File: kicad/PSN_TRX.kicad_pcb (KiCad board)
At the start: 4 copper layers, 220 x 150 mm, 161 parts, among them IC1 LP2950L-5.0V, IC2 NJM2904, J1 PWR_IN, K1 G5V-2, Q1 3SK59, Q10 2SK439, Q11 2SC1815, Q12 2SC1815, Q13 2SC1815, Q14 2SK439, Q15 2SC1815, Q17 2SC1815, Q2 2SC1923, Q3 2SC1815, Q4 2SC1815, Q5 2SC2120, Q6 2SA950, Q7 2SC1923, Q8 2SC1923, Q9 2SK439, SW1 SW, T1 ST-71, X1 50.5MHz/3

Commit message: KiCad: シンボル統合・パネル部品除外・PCBクリーンアップ
- 外部シンボルファイル4本をPSN_TRX.kicad_symに統合
  (Arduino_Nano_R4_Socket, Si5351_DIP8, Si5351A, AE-LCNV4-MOSFET)
  → sym-lib-tableはPSN_TRXライブラリのみに統一
- SW1, SW2, R13, LED1をon_board=noに変更（パネル取付部品）
- PCBからSW1, R13, LED1フットプリントを削除（SW2は元から未配置）
- .gitignoreに_restore_backup_*/を追加

Co-Authored-By: Claude Sonnet 4.6 <noreply@anthropic.com>
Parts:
- removed LED1: LED, PinHeader_1x02_P2.54mm_Vertical
- removed R13: 1k, R_Axial_DIN0207_L6.3mm_D2.5mm_P2.54mm_Vertical
- removed SW1: SW, SW_DIP_SPSTx01_Slide_6.7x4.1mm_W7.62mm_P2.54mm_LowProfile

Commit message: KiCad: VR1・VR2をパネル取付に変更（on_board=no、PCBから削除）
Co-Authored-By: Claude Sonnet 4.6 <noreply@anthropic.com>
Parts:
- removed VR1: 5k, PinHeader_1x03_P2.54mm_Vertical
- removed VR2: 10k, PinHeader_1x03_P2.54mm_Vertical

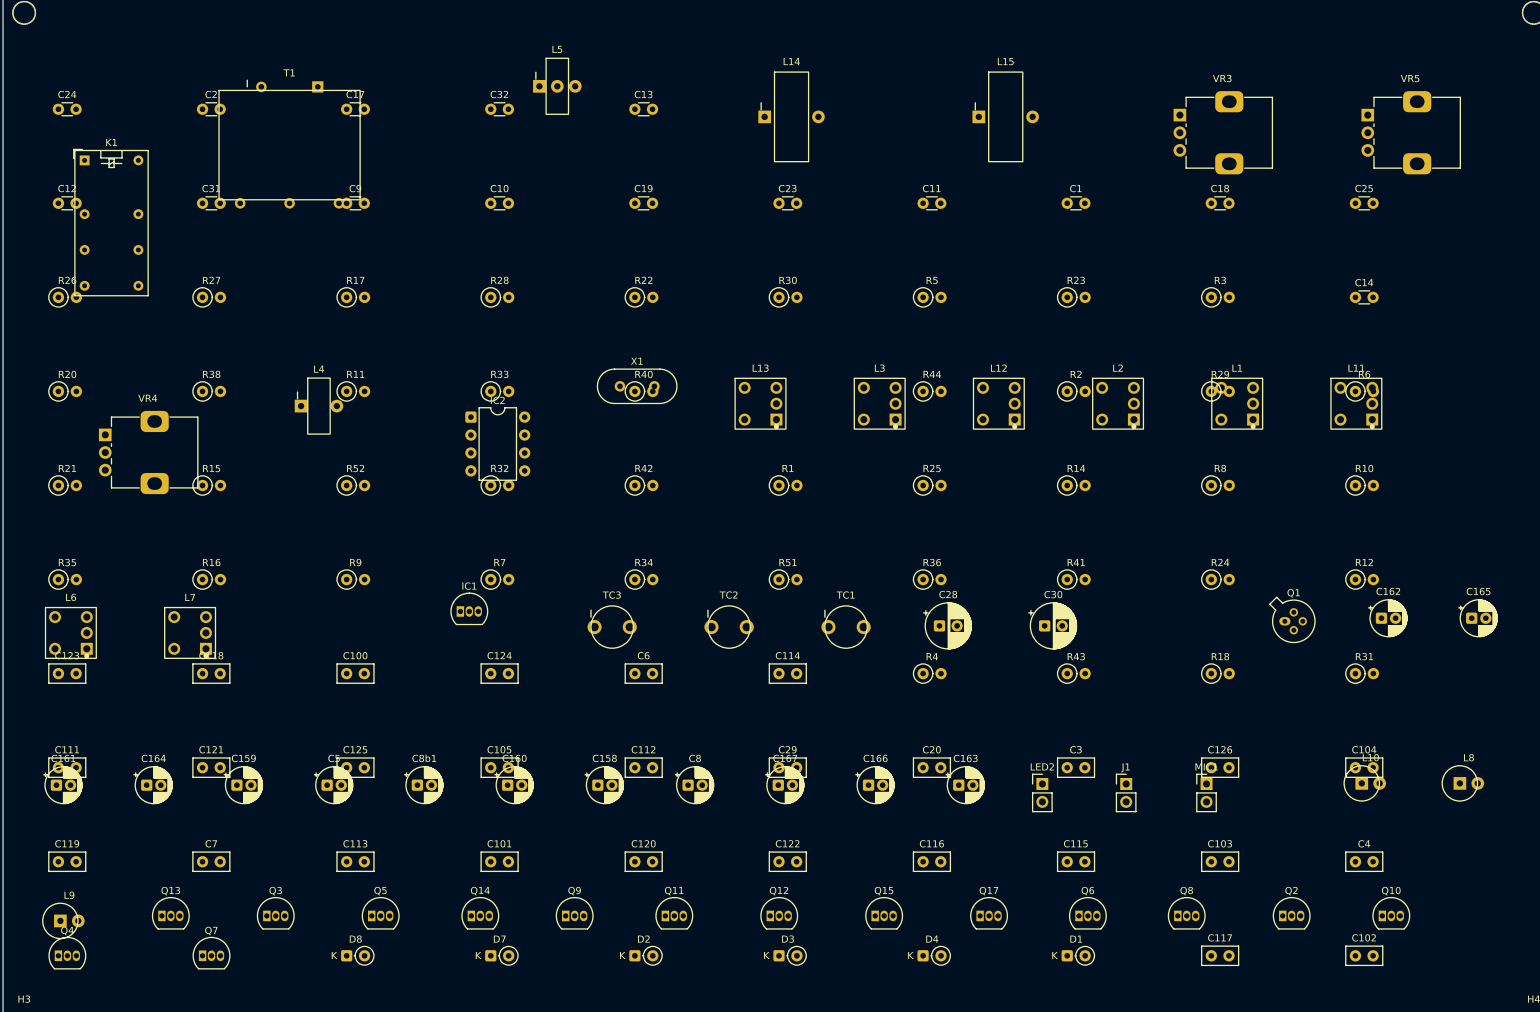
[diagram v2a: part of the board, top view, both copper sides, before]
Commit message: feat: GF063Pポテンショメータのカスタムシンボル追加・フットプリント修正、VR3-7をPSN_TRXライブラリに移行
- PSN_TRX:Potentiometer_GF063P シンボルをシンボルライブラリに追加（VRプレフィックス、フットプリント紐付け済み）
- Potentiometer_TOCOS_GF063P_Vertical フットプリントのピン配置をデータシートに基づき修正
  - 旧: ピン1・2・3が一直線（誤り）
  - 新: 三角配置（ピン2ワイパーを2.5mm上方にオフセット）
- VR3〜VR7のシンボル参照を Device:R_Potentiometer → PSN_TRX:Potentiometer_GF063P に変更

Co-Authored-By: Claude Sonnet 4.6 <noreply@anthropic.com>
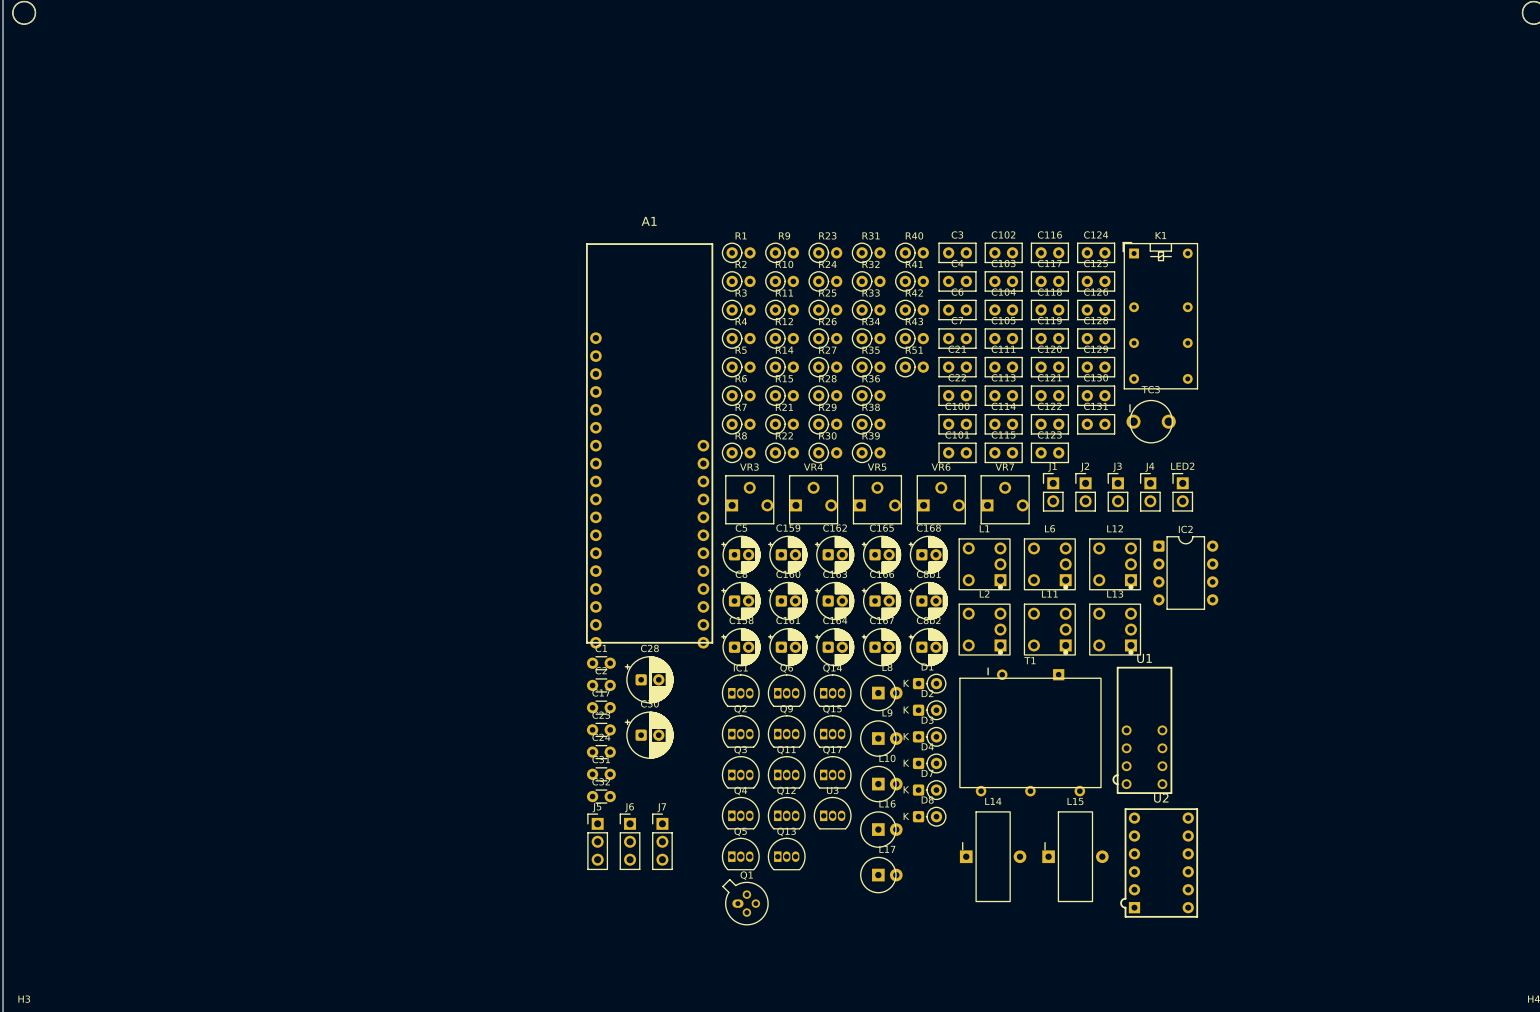
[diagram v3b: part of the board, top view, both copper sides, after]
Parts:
- removed C10, C9: 100p, C_Disc_D3.0mm_W1.6mm_P2.50mm
- removed C11, C12, C14: 47p, C_Disc_D3.0mm_W1.6mm_P2.50mm
- removed C112: 0.01u, C_Disc_D5.0mm_W2.5mm_P2.50mm
- removed C13: 5p, C_Disc_D3.0mm_W1.6mm_P2.50mm
- removed C18: 15p, C_Disc_D3.0mm_W1.6mm_P2.50mm
- removed C19, C25: 33p, C_Disc_D3.0mm_W1.6mm_P2.50mm
- removed C20, C29: 0.001u, C_Disc_D5.0mm_W2.5mm_P2.50mm
- removed L3, L7: 7T50, L_FCZ07S_CT
- removed L4: T-30-10 6T/0.4mm, L_T30_2pin_Vertical
- removed L5: T-30-10 6T+1T/0.4mm, L_T30_3pin_Vertical
- removed MIC1: MIC, PinHeader_1x02_P2.54mm_Vertical
- removed Q10: 2SK439, TO-92_Inline
- removed Q7, Q8: 2SC1923, TO-92_Inline
- removed R16: 10k, R_Axial_DIN0207_L6.3mm_D2.5mm_P2.54mm_Vertical
- removed R17, R20: 100k, R_Axial_DIN0207_L6.3mm_D2.5mm_P2.54mm_Vertical
- removed R18: 1k, R_Axial_DIN0207_L6.3mm_D2.5mm_P2.54mm_Vertical
- removed R44: 100, R_Axial_DIN0207_L6.3mm_D2.5mm_P2.54mm_Vertical
- removed R52: 51, R_Axial_DIN0207_L6.3mm_D2.5mm_P2.54mm_Vertical
- removed TC1, TC2: 40p, C_Trimmer_TMCV01
- removed X1: 50.5MHz/3, Crystal_HC49-4H_Vertical
- added A1: Arduino_Nano_R4_Socket, PSN_TRX:Arduino_Nano_R4_Socket, F.Cu at (96.7, 69.4)
- added C128: 47PF, Capacitor_THT:C_Disc_D5.0mm_W2.5mm_P2.50mm, F.Cu at (158.7, 54.2)
- added C129: 47PF, Capacitor_THT:C_Disc_D5.0mm_W2.5mm_P2.50mm, F.Cu at (158.7, 58.2)
- added C130: 47PF, Capacitor_THT:C_Disc_D5.0mm_W2.5mm_P2.50mm, F.Cu at (158.7, 62.3)
- added C131: 47PF, Capacitor_THT:C_Disc_D5.0mm_W2.5mm_P2.50mm, F.Cu at (158.7, 66.3)
- added C168: 1u, Capacitor_THT:CP_Radial_D5.0mm_P2.00mm, F.Cu at (135.3, 84.8)
- added C21: 0.001u, Capacitor_THT:C_Disc_D5.0mm_W2.5mm_P2.50mm, F.Cu at (139.1, 58.2)
- added C22: 0.001u, Capacitor_THT:C_Disc_D5.0mm_W2.5mm_P2.50mm, F.Cu at (139.1, 62.3)
- added C8b2: 10u, Capacitor_THT:CP_Radial_D5.0mm_P2.00mm, F.Cu at (135.3, 97.9)
- added J2: SP-OUT, Connector_PinHeader_2.54mm:PinHeader_1x02_P2.54mm_Vertical, F.Cu at (158.5, 74.7)
- added J3: RF-IN, Connector_PinHeader_2.54mm:PinHeader_1x02_P2.54mm_Vertical, F.Cu at (163.1, 74.7)
- added J4: MIC-IN, Connector_PinHeader_2.54mm:PinHeader_1x02_P2.54mm_Vertical, F.Cu at (167.6, 74.7)
- added J5: I2C_OUT, Connector_PinHeader_2.54mm:PinHeader_1x03_P2.54mm_Vertical, F.Cu at (89.3, 123.0)
- added J6: Volume, Connector_PinHeader_2.54mm:PinHeader_1x03_P2.54mm_Vertical, F.Cu at (93.9, 123.0)
- added J7: Volume, Connector_PinHeader_2.54mm:PinHeader_1x03_P2.54mm_Vertical, F.Cu at (98.5, 123.0)
- added L16: 100nH, PSN_TRX:L_AL0510-153K_Vertical, F.Cu at (129.1, 123.8)
- added L17: 100nH, PSN_TRX:L_AL0510-153K_Vertical, F.Cu at (129.1, 130.2)
- added R39: 51, Resistor_THT:R_Axial_DIN0207_L6.3mm_D2.5mm_P2.54mm_Vertical, F.Cu at (126.8, 70.4)
- added U1: Si5351_DIP8, PSN_TRX:DIP-8_W7.62mm, F.Cu at (166.8, 109.7)
- added U2: AE-LCNV4-MOSFET, PSN_TRX:DIP-12_W7.62mm, F.Cu at (169.2, 122.1)
- added U3: LP2950-3.3_TO92, Package_TO_SOT_THT:TO-92_Inline, F.Cu at (121.3, 121.8)
- added VR6: 500, PSN_TRX:Potentiometer_TOCOS_GF063P_Vertical, F.Cu at (135.5, 77.8)
- added VR7: 500, PSN_TRX:Potentiometer_TOCOS_GF063P_Vertical, F.Cu at (144.6, 77.8)
- C1, C17, C2, C23, C24, C31, C32: footprint C_Disc_D3.0mm_W1.6mm_P2.50mm -> Capacitor_THT:C_Disc_D3.0mm_W1.6mm_P2.50mm
- C100, C101, C103, C111, C113, C114, C115, C116, C117, C118, C119, C120, C121, C124, C125, C126, C3, C4, C6, C7: footprint C_Disc_D5.0mm_W2.5mm_P2.50mm -> Capacitor_THT:C_Disc_D5.0mm_W2.5mm_P2.50mm
- C102, C104, C105, C122, C123: value 0.01u -> 1u; footprint C_Disc_D5.0mm_W2.5mm_P2.50mm -> Capacitor_THT:C_Disc_D5.0mm_W2.5mm_P2.50mm
- C158, C159, C160, C161, C162, C163, C164, C165, C166, C167, C5, C8, C8b1: footprint CP_Radial_D5.0mm_P2.00mm -> Capacitor_THT:CP_Radial_D5.0mm_P2.00mm
- C28, C30: footprint CP_Radial_D6.3mm_P2.50mm -> Capacitor_THT:CP_Radial_D6.3mm_P2.50mm
- D1, D2, D3, D4, D7, D8: footprint D_DO-35_SOD27_P2.54mm_Vertical_CathodeUp -> Diode_THT:D_DO-35_SOD27_P2.54mm_Vertical_CathodeUp
- IC1, Q11, Q12, Q13, Q14, Q15, Q17, Q2, Q3, Q4, Q5, Q6, Q9: footprint TO-92_Inline -> Package_TO_SOT_THT:TO-92_Inline
- IC2: footprint DIP-8_W7.62mm -> Package_DIP:DIP-8_W7.62mm
- J1, LED2: footprint PinHeader_1x02_P2.54mm_Vertical -> Connector_PinHeader_2.54mm:PinHeader_1x02_P2.54mm_Vertical
- K1: footprint Relay_DPDT_Omron_G5V-2 -> Relay_THT:Relay_DPDT_Omron_G5V-2
- L1, L11, L12, L13, L2, L6: footprint L_FCZ07S_CT -> PSN_TRX:L_FCZ07S_CT
- L10, L8, L9: footprint L_AL0510-153K_Vertical -> PSN_TRX:L_AL0510-153K_Vertical
- L14, L15: footprint L_T50_2pin_Vertical -> PSN_TRX:L_T50_2pin_Vertical
- Q1: footprint TO-72-4 -> Package_TO_SOT_THT:TO-72-4
- R1, R10, R11, R12, R14, R15, R2, R22, R23, R24, R25, R26, R27, R3, R33, R35, R36, R38, R4, R40, R41, R42, R43, R5, R51, R6, R7, R8, R9: footprint R_Axial_DIN0207_L6.3mm_D2.5mm_P2.54mm_Vertical -> Resistor_THT:R_Axial_DIN0207_L6.3mm_D2.5mm_P2.54mm_Vertical
- R21: value 220k -> 47; footprint R_Axial_DIN0207_L6.3mm_D2.5mm_P2.54mm_Vertical -> Resistor_THT:R_Axial_DIN0207_L6.3mm_D2.5mm_P2.54mm_Vertical
- R28, R31: value 100k -> 1M; footprint R_Axial_DIN0207_L6.3mm_D2.5mm_P2.54mm_Vertical -> Resistor_THT:R_Axial_DIN0207_L6.3mm_D2.5mm_P2.54mm_Vertical
- R29: value 330 -> 4.7k; footprint R_Axial_DIN0207_L6.3mm_D2.5mm_P2.54mm_Vertical -> Resistor_THT:R_Axial_DIN0207_L6.3mm_D2.5mm_P2.54mm_Vertical
- R30: value 1k -> 330; footprint R_Axial_DIN0207_L6.3mm_D2.5mm_P2.54mm_Vertical -> Resistor_THT:R_Axial_DIN0207_L6.3mm_D2.5mm_P2.54mm_Vertical
- R32: value 1k -> 4.7k; footprint R_Axial_DIN0207_L6.3mm_D2.5mm_P2.54mm_Vertical -> Resistor_THT:R_Axial_DIN0207_L6.3mm_D2.5mm_P2.54mm_Vertical
- R34: value 100 -> 47; footprint R_Axial_DIN0207_L6.3mm_D2.5mm_P2.54mm_Vertical -> Resistor_THT:R_Axial_DIN0207_L6.3mm_D2.5mm_P2.54mm_Vertical
- T1: footprint Transformer_ST71_CB19 -> PSN_TRX:Transformer_ST71_CB19
- TC3: footprint C_Trimmer_TMCV01 -> PSN_TRX:C_Trimmer_TMCV01
- VR3, VR4, VR5: footprint Potentiometer_Alps_RK09K_Single_Vertical -> PSN_TRX:Potentiometer_TOCOS_GF063P_Vertical
- moved C119 157.8 mm to (152.2, 54.2)
- moved K1 149.3 mm to (165.3, 42.1)
- moved C111 144.4 mm to (145.6, 58.2)
- moved C123 142.8 mm to (152.2, 70.4)
- moved L6 139.1 mm to (153.4, 86.2)
- moved T1 134.1 mm to (150.6, 110.1)
- moved C121 130.0 mm to (152.2, 62.3)
- moved C118 129.6 mm to (152.2, 50.1)
- moved C7 129.2 mm to (139.1, 54.2)
- moved C125 125.6 mm to (158.7, 46.1)
- moved L9 118.8 mm to (129.1, 110.9)
- moved C24 118.5 mm to (88.6, 112.8)
- moved R35 117.8 mm to (126.8, 58.2)
- moved C113 113.2 mm to (145.6, 62.3)
- moved C102 112.0 mm to (145.6, 42.0)
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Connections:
- C1 pad 1: (no net) -> Net-(L1-SA)
- C1 pad 2: (no net) -> GND
- C100 pad 1: (no net) -> Net-(J7-Pin_2)
- C100 pad 2: (no net) -> GND
- C101 pad 1: (no net) -> Net-(L2-SA)
- C101 pad 2: (no net) -> Net-(Q2-B)
- C102 pad 1: (no net) -> Net-(Q2-C)
- C102 pad 2: (no net) -> Net-(Q3-B)
- C103 pad 1: (no net) -> Net-(Q1-S)
- C103 pad 2: (no net) -> GND
- C104 pad 1: (no net) -> Net-(Q3-C)
- C104 pad 2: (no net) -> Net-(C104-Pad2)
- C105 pad 1: (no net) -> Net-(Q4-C)
- C105 pad 2: (no net) -> Net-(C105-Pad2)
- C111 pad 1: (no net) -> Net-(Q9-S)
- C111 pad 2: (no net) -> GND
- C113 pad 1: (no net) -> Net-(L6-SB)
- C113 pad 2: (no net) -> GND
- C114 pad 1: (no net) -> Net-(Q9-G)
- C114 pad 2: (no net) -> Net-(C114-Pad2)
- C115 pad 1: (no net) -> Net-(C115-Pad1)
- C115 pad 2: (no net) -> Net-(U1-CLK0)
- C116 pad 1: (no net) -> Net-(C116-Pad1)
- C116 pad 2: (no net) -> Net-(U1-CLK1)
- C117 pad 1: (no net) -> Net-(Q14-S)
- C117 pad 2: (no net) -> GND
- C118 pad 1: (no net) -> Net-(L12-SB)
- C118 pad 2: (no net) -> GND
- C119 pad 1: (no net) -> Net-(Q12-B)
- C119 pad 2: (no net) -> Net-(L12-AA)
- C120 pad 1: (no net) -> Net-(C120-Pad1)
- C120 pad 2: (no net) -> GND
- C121 pad 1: (no net) -> +9V
- C121 pad 2: (no net) -> GND
- C122 pad 1: (no net) -> Net-(J6-Pin_2)
- C122 pad 2: (no net) -> Net-(Q5-B)
- C123 pad 1: (no net) -> Net-(Q6-B)
- C123 pad 2: (no net) -> Net-(J6-Pin_2)
- C124 pad 1: (no net) -> Net-(C124-Pad1)
- C124 pad 2: (no net) -> GND
- C125 pad 1: (no net) -> Net-(Q12-E)
- C125 pad 2: (no net) -> GND
- C126 pad 1: (no net) -> Net-(L12-SB)
- C126 pad 2: (no net) -> GND
- C158 pad 1: (no net) -> Net-(Q13-B)
- C158 pad 2: (no net) -> Net-(C158-Pad2)
- C159 pad 1: (no net) -> Net-(C159-Pad1)
- C159 pad 2: (no net) -> Net-(Q11-C)
- C160 pad 1: (no net) -> Net-(Q11-B)
- C160 pad 2: (no net) -> Net-(J4-Pin_1)
- C161 pad 1: (no net) -> Net-(C159-Pad1)
- C161 pad 2: (no net) -> GND
- C162 pad 1: (no net) -> Net-(T1-AA)
- C162 pad 2: (no net) -> Net-(C162-Pad2)
- C163 pad 1: (no net) -> Net-(C162-Pad2)
- C163 pad 2: (no net) -> GND
- C164 pad 1: (no net) -> Net-(C164-Pad1)
- C164 pad 2: (no net) -> Net-(T1-SB)
- C165 pad 1: (no net) -> Net-(Q17-B)
- C165 pad 2: (no net) -> Net-(T1-SA)
- C166 pad 1: (no net) -> Net-(C120-Pad1)
- C166 pad 2: (no net) -> Net-(Q17-C)
- C167 pad 1: (no net) -> Net-(C124-Pad1)
- C167 pad 2: (no net) -> Net-(Q13-C)
- C17 pad 1: (no net) -> Net-(L6-SA)
- C17 pad 2: (no net) -> Net-(L6-SB)
- C2 pad 1: (no net) -> Net-(L2-AA)
- C2 pad 2: (no net) -> +9V
- C23 pad 1: (no net) -> Net-(D1-A)
- C23 pad 2: (no net) -> Net-(D2-K)
- C24 pad 1: (no net) -> Net-(L12-SA)
- C24 pad 2: (no net) -> Net-(L12-SB)
- C28 pad 1: (no net) -> Net-(Q5-C)
- C28 pad 2: (no net) -> /PHONE
- C3 pad 1: (no net) -> Net-(Q2-E)
- C3 pad 2: (no net) -> Net-(L6-AA)
- C30 pad 1: (no net) -> Net-(Q6-E)
- C30 pad 2: (no net) -> GND
- C31 pad 1: (no net) -> Net-(L13-SA)
- C31 pad 2: (no net) -> Net-(L12-SB)
- C32 pad 1: (no net) -> Net-(C32-Pad1)
- C32 pad 2: (no net) -> Net-(D7-A)
- C4 pad 1: (no net) -> Net-(C104-Pad2)
- C4 pad 2: (no net) -> GND
- C5 pad 1: (no net) -> +9V
- C5 pad 2: (no net) -> GND
- C6 pad 1: (no net) -> Net-(Q4-B)
- C6 pad 2: (no net) -> GND
- C7 pad 1: (no net) -> Net-(Q4-E)
- C7 pad 2: (no net) -> GND
- C8 pad 1: (no net) -> +9V
- C8 pad 2: (no net) -> GND
- C8b1 pad 1: (no net) -> +5V
- C8b1 pad 2: (no net) -> GND
- D1 pad 1: (no net) -> Net-(D1-K)
- D1 pad 2: (no net) -> Net-(D1-A)
- D2 pad 1: (no net) -> Net-(D2-K)
- D2 pad 2: (no net) -> Net-(D2-A)
- D3 pad 1: (no net) -> Net-(D3-K)
- D3 pad 2: (no net) -> Net-(D1-A)
- D4 pad 1: (no net) -> Net-(D2-K)
- D4 pad 2: (no net) -> Net-(D4-A)
- D7 pad 1: (no net) -> Net-(D7-K)
- D7 pad 2: (no net) -> Net-(D7-A)
- D8 pad 1: (no net) -> Net-(D7-A)
- D8 pad 2: (no net) -> GND
- IC1 pad 1: (no net) -> +5V
- IC1 pad 2: (no net) -> GND
- IC1 pad 3: (no net) -> +9V
- IC2 pad 1: (no net) -> Net-(C158-Pad2)
- IC2 pad 2: (no net) -> Net-(IC2A--)
- IC2 pad 3: (no net) -> Net-(IC2A-+)
- IC2 pad 4: (no net) -> GND
- IC2 pad 5: (no net) -> GND
- IC2 pad 6: (no net) -> Net-(IC2B--)
- IC2 pad 7: (no net) -> Net-(IC2B--)
- IC2 pad 8: (no net) -> +5V
- J1 pad 1: (no net) -> Net-(J1-Pin_1)
- J1 pad 2: (no net) -> GND
- K1 pad 1: (no net) -> +5V
- K1 pad 11: (no net) -> +9V
- K1 pad 13: (no net) -> Net-(J3-Pin_1)
- K1 pad 16: (no net) -> Net-(K1-Pad16)
- K1 pad 4: (no net) -> Net-(J1-Pin_1)
- K1 pad 6: (no net) -> Net-(L1-AA)
- K1 pad 8: (no net) -> Net-(C32-Pad1)
- K1 pad 9: (no net) -> Net-(L12-SB)
- L1 pad 1: (no net) -> Net-(L1-SA)
- L1 pad 2: (no net) -> unconnected-(L1-CT-Pad2)
- L1 pad 3: (no net) -> GND
- L1 pad 4: (no net) -> Net-(L1-AA)
- L1 pad 5: (no net) -> GND
- L10 pad 1: (no net) -> Net-(C22-Pad2)
- L10 pad 2: (no net) -> Net-(C124-Pad1)
- L11 pad 1: (no net) -> Net-(D1-A)
- L11 pad 2: (no net) -> unconnected-(L11-CT-Pad2)
- L11 pad 3: (no net) -> Net-(D2-K)
- L11 pad 4: (no net) -> Net-(L11-AA)
- L11 pad 5: (no net) -> GND
- L12 pad 1: (no net) -> Net-(L12-SA)
- L12 pad 2: (no net) -> unconnected-(L12-CT-Pad2)
- L12 pad 3: (no net) -> Net-(L12-SB)
- L12 pad 4: (no net) -> Net-(L12-AA)
- L12 pad 5: (no net) -> GND
- L13 pad 1: (no net) -> Net-(L13-SA)
- L13 pad 2: (no net) -> Net-(L13-CT)
- L13 pad 3: (no net) -> Net-(L12-SB)
- L13 pad 4: (no net) -> Net-(L13-AA)
- L13 pad 5: (no net) -> GND
- L14 pad 1: (no net) -> Net-(L14-Pad1)
- L14 pad 2: (no net) -> Net-(L13-AA)
- L15 pad 1: (no net) -> Net-(C32-Pad1)
- L15 pad 2: (no net) -> Net-(L14-Pad1)
- L2 pad 1: (no net) -> Net-(L2-SA)
- L2 pad 2: (no net) -> unconnected-(L2-CT-Pad2)
- L2 pad 3: (no net) -> GND
- L2 pad 4: (no net) -> Net-(L2-AA)
- L2 pad 5: (no net) -> +9V
- L6 pad 1: (no net) -> Net-(L6-SA)
- L6 pad 2: (no net) -> unconnected-(L6-CT-Pad2)
- L6 pad 3: (no net) -> Net-(L6-SB)
- L6 pad 4: (no net) -> Net-(L6-AA)
- L6 pad 5: (no net) -> GND
- L8 pad 1: (no net) -> Net-(C162-Pad2)
- L8 pad 2: (no net) -> Net-(C159-Pad1)
- L9 pad 1: (no net) -> Net-(C21-Pad2)
- L9 pad 2: (no net) -> Net-(C120-Pad1)
- LED2 pad 1: (no net) -> Net-(LED2-K)
- LED2 pad 2: (no net) -> Net-(L12-SB)
- Q1 pad 1: (no net) -> Net-(L2-AA)
- Q1 pad 2: (no net) -> Net-(Q1-S)
- Q1 pad 3: (no net) -> Net-(L1-SA)
- Q1 pad 4: (no net) -> Net-(J7-Pin_2)
- Q11 pad 1: (no net) -> Net-(Q11-B)
- Q11 pad 2: (no net) -> Net-(Q11-C)
- Q11 pad 3: (no net) -> Net-(Q11-E)
- Q12 pad 1: (no net) -> Net-(Q12-B)
- Q12 pad 2: (no net) -> Net-(L13-CT)
- Q12 pad 3: (no net) -> Net-(Q12-E)
- Q13 pad 1: (no net) -> Net-(Q13-B)
- Q13 pad 2: (no net) -> Net-(Q13-C)
- Q13 pad 3: (no net) -> Net-(Q13-E)
- Q14 pad 1: (no net) -> Net-(L11-AA)
- Q14 pad 2: (no net) -> Net-(L12-SA)
- Q14 pad 3: (no net) -> Net-(Q14-S)
- Q15 pad 1: (no net) -> Net-(D7-K)
- Q15 pad 2: (no net) -> Net-(LED2-K)
- Q15 pad 3: (no net) -> GND
- Q17 pad 1: (no net) -> Net-(Q17-B)
- Q17 pad 2: (no net) -> Net-(Q17-C)
- Q17 pad 3: (no net) -> Net-(Q17-E)
- Q2 pad 1: (no net) -> Net-(Q2-B)
- Q2 pad 2: (no net) -> Net-(Q2-C)
- Q2 pad 3: (no net) -> Net-(Q2-E)
- Q3 pad 1: (no net) -> Net-(Q3-B)
- Q3 pad 2: (no net) -> Net-(Q3-C)
- Q3 pad 3: (no net) -> GND
- Q4 pad 1: (no net) -> Net-(Q4-B)
- Q4 pad 2: (no net) -> Net-(Q4-C)
- Q4 pad 3: (no net) -> Net-(Q4-E)
- Q5 pad 1: (no net) -> Net-(Q5-B)
- Q5 pad 2: (no net) -> Net-(Q5-C)
- Q5 pad 3: (no net) -> GND
- Q6 pad 1: (no net) -> Net-(Q6-B)
- Q6 pad 2: (no net) -> Net-(Q5-C)
- Q6 pad 3: (no net) -> Net-(Q6-E)
- Q9 pad 1: (no net) -> Net-(Q9-G)
- Q9 pad 2: (no net) -> Net-(L6-SA)
- Q9 pad 3: (no net) -> Net-(Q9-S)
- R1 pad 1: (no net) -> Net-(Q1-S)
- R1 pad 2: (no net) -> GND
- R10 pad 1: (no net) -> Net-(Q4-C)
- R10 pad 2: (no net) -> +9V
- R11 pad 1: (no net) -> Net-(Q5-B)
- R11 pad 2: (no net) -> Net-(Q5-C)
- R12 pad 1: (no net) -> Net-(Q5-C)
- R12 pad 2: (no net) -> Net-(Q6-B)
- R14 pad 1: (no net) -> Net-(J7-Pin_1)
- R14 pad 2: (no net) -> +9V
- R15 pad 1: (no net) -> Net-(Q6-E)
- R15 pad 2: (no net) -> +9V
- R2 pad 1: (no net) -> Net-(Q2-B)
- R2 pad 2: (no net) -> +9V
- R21 pad 1: (no net) -> Net-(C114-Pad2)
- R21 pad 2: (no net) -> GND
- R22 pad 1: (no net) -> Net-(L12-SB)
- R22 pad 2: (no net) -> Net-(J4-Pin_1)
- R23 pad 1: (no net) -> Net-(Q11-C)
- R23 pad 2: (no net) -> Net-(Q11-B)
- R24 pad 1: (no net) -> Net-(L12-SB)
- R24 pad 2: (no net) -> Net-(Q11-C)
- R25 pad 1: (no net) -> Net-(Q11-E)
- R25 pad 2: (no net) -> GND
- R26 pad 1: (no net) -> Net-(IC2A-+)
- R26 pad 2: (no net) -> Net-(C164-Pad1)
- R27 pad 1: (no net) -> Net-(C158-Pad2)
- R27 pad 2: (no net) -> Net-(IC2A-+)
- R28 pad 1: (no net) -> Net-(Q13-C)
- R28 pad 2: (no net) -> Net-(Q13-B)
- R29 pad 1: (no net) -> Net-(L12-SB)
- R29 pad 2: (no net) -> Net-(Q13-C)
- R3 pad 1: (no net) -> Net-(Q2-E)
- R3 pad 2: (no net) -> GND
- R30 pad 1: (no net) -> Net-(Q13-E)
- R30 pad 2: (no net) -> GND
- R31 pad 1: (no net) -> Net-(Q17-C)
- R31 pad 2: (no net) -> Net-(Q17-B)
- R32 pad 1: (no net) -> Net-(L12-SB)
- R32 pad 2: (no net) -> Net-(Q17-C)
- R33 pad 1: (no net) -> Net-(Q17-E)
- R33 pad 2: (no net) -> GND
- R34 pad 1: (no net) -> Net-(C22-Pad1)
- R34 pad 2: (no net) -> GND
- R35 pad 1: (no net) -> Net-(L12-SB)
- R35 pad 2: (no net) -> Net-(Q12-B)
- R36 pad 1: (no net) -> Net-(Q14-S)
- R36 pad 2: (no net) -> GND
- R38 pad 1: (no net) -> Net-(Q12-B)
- R38 pad 2: (no net) -> GND
- R4 pad 1: (no net) -> Net-(C104-Pad2)
- R4 pad 2: (no net) -> Net-(Q4-B)
- R40 pad 1: (no net) -> Net-(LED2-K)
- R40 pad 2: (no net) -> Net-(L12-SB)
- R41 pad 1: (no net) -> Net-(D7-K)
- R41 pad 2: (no net) -> GND
- R42 pad 1: (no net) -> Net-(Q9-G)
- R42 pad 2: (no net) -> GND
- R43 pad 1: (no net) -> Net-(C105-Pad2)
- R43 pad 2: (no net) -> Net-(J6-Pin_1)
- R5 pad 1: (no net) -> Net-(Q2-C)
- R5 pad 2: (no net) -> +9V
- R51 pad 1: (no net) -> Net-(Q9-S)
- R51 pad 2: (no net) -> GND
- R6 pad 1: (no net) -> Net-(Q3-B)
- R6 pad 2: (no net) -> Net-(Q3-C)
- R7 pad 1: (no net) -> Net-(Q3-C)
- R7 pad 2: (no net) -> +9V
- R8 pad 1: (no net) -> Net-(Q4-B)
- R8 pad 2: (no net) -> Net-(Q4-C)
- R9 pad 1: (no net) -> Net-(Q4-E)
- R9 pad 2: (no net) -> GND
- T1 pad 1: (no net) -> Net-(T1-AA)
- T1 pad 2: (no net) -> GND
- T1 pad 3: (no net) -> Net-(T1-SA)
- T1 pad 4: (no net) -> GND
- T1 pad 5: (no net) -> Net-(T1-SB)
- TC3 pad 1: (no net) -> Net-(L14-Pad1)
- TC3 pad 2: (no net) -> GND
- VR3 pad 1: (no net) -> Net-(IC2A--)
- VR3 pad 2: (no net) -> Net-(C164-Pad1)
- VR3 pad 3: (no net) -> Net-(C164-Pad1)
- VR4 pad 1: (no net) -> Net-(D1-K)
- VR4 pad 2: (no net) -> Net-(C21-Pad2)
- VR4 pad 3: (no net) -> Net-(D2-A)
- VR5 pad 1: (no net) -> Net-(D3-K)
- VR5 pad 2: (no net) -> Net-(C22-Pad2)
- VR5 pad 3: (no net) -> Net-(D4-A)

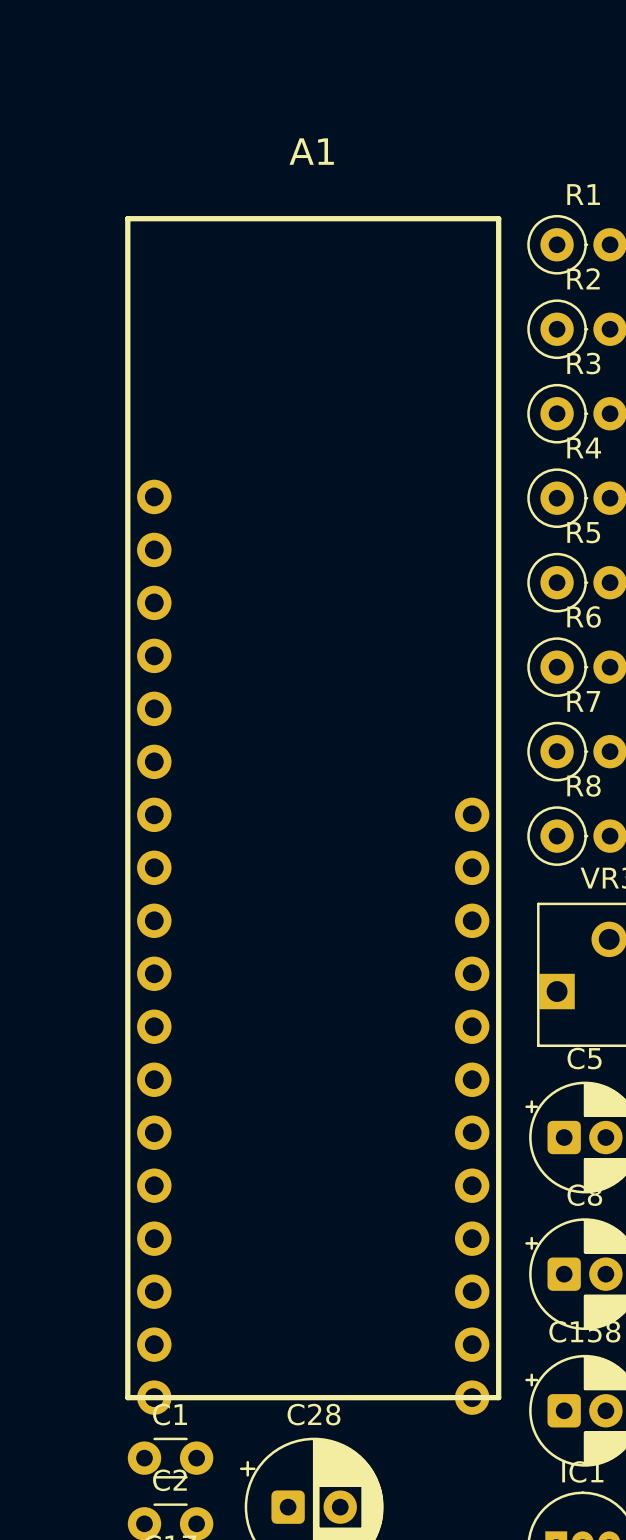
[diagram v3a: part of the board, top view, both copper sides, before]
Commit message: fix: PCBのA1フットプリントをNano R4からSeeeduino XIAO Socketに置き換え
- Arduino_Nano_R4_Socket (30pin) → Seeeduino_XIAO_Socket (14pin)
- 座標 (96.665, 69.355) を維持
- 回路図シンボルUUID (ee810141-...) にパスを更新

Co-Authored-By: Claude Sonnet 4.6 <noreply@anthropic.com>
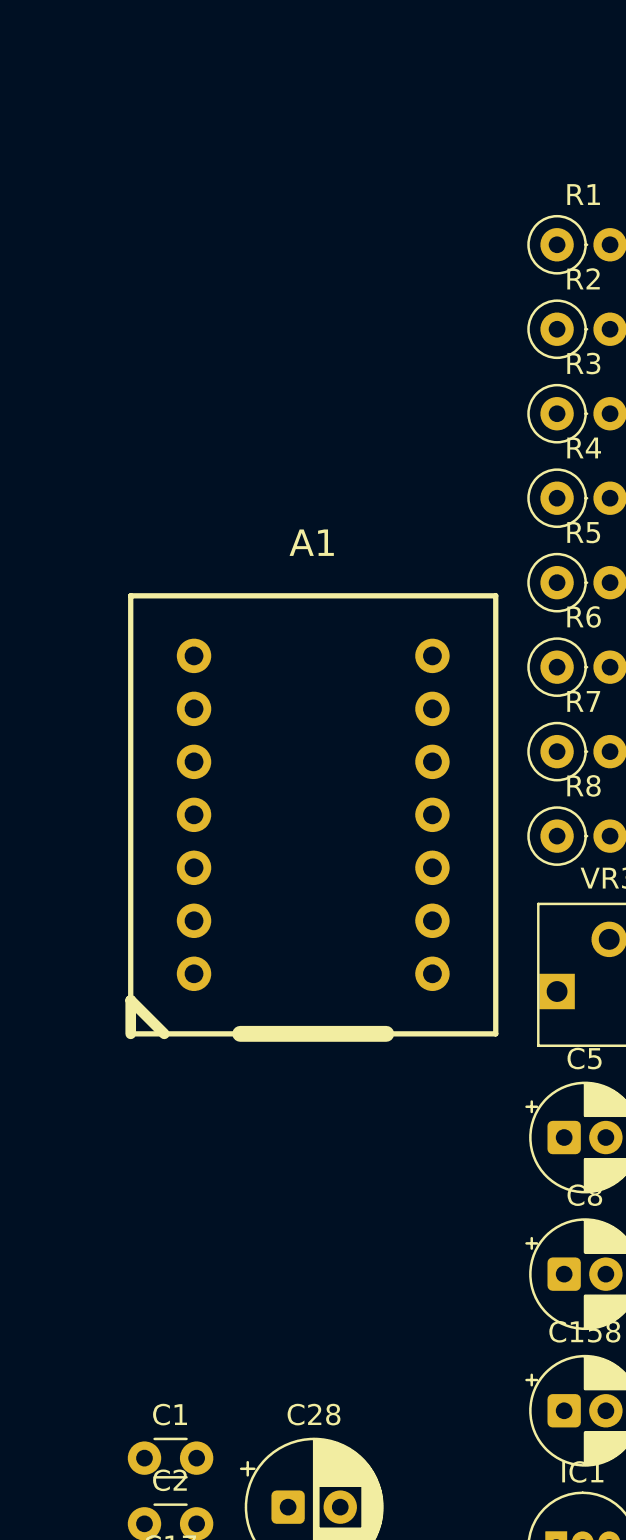
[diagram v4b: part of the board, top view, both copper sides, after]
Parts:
- A1: value Arduino_Nano_R4_Socket -> Seeeduino_XIAO_Socket; footprint PSN_TRX:Arduino_Nano_R4_Socket -> PSN_TRX:Seeeduino_XIAO_Socket
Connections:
- A1 pad 1: unconnected-(A1-D1/TX-Pad1)_1 -> (no net)
- A1 pad 10: unconnected-(A1-D8-Pad10) -> (no net)
- A1 pad 11: unconnected-(A1-D9-Pad11) -> (no net)
- A1 pad 12: unconnected-(A1-D10/SS-Pad12) -> (no net)
- A1 pad 13: unconnected-(A1-D11/MOSI-Pad13) -> (no net)
- A1 pad 14: unconnected-(A1-D12/MISO-Pad14) -> (no net)
- A1 pad 2: unconnected-(A1-D0/RX-Pad2) -> (no net)
- A1 pad 3: unconnected-(A1-GND-Pad3) -> (no net)
- A1 pad 4: unconnected-(A1-D2-Pad4) -> (no net)
- A1 pad 5: unconnected-(A1-D3-Pad5) -> (no net)
- A1 pad 6: unconnected-(A1-D4-Pad6) -> (no net)
- A1 pad 7: unconnected-(A1-D5-Pad7) -> (no net)
- A1 pad 8: unconnected-(A1-D6-Pad8) -> (no net)
- A1 pad 9: unconnected-(A1-D7-Pad9) -> (no net)

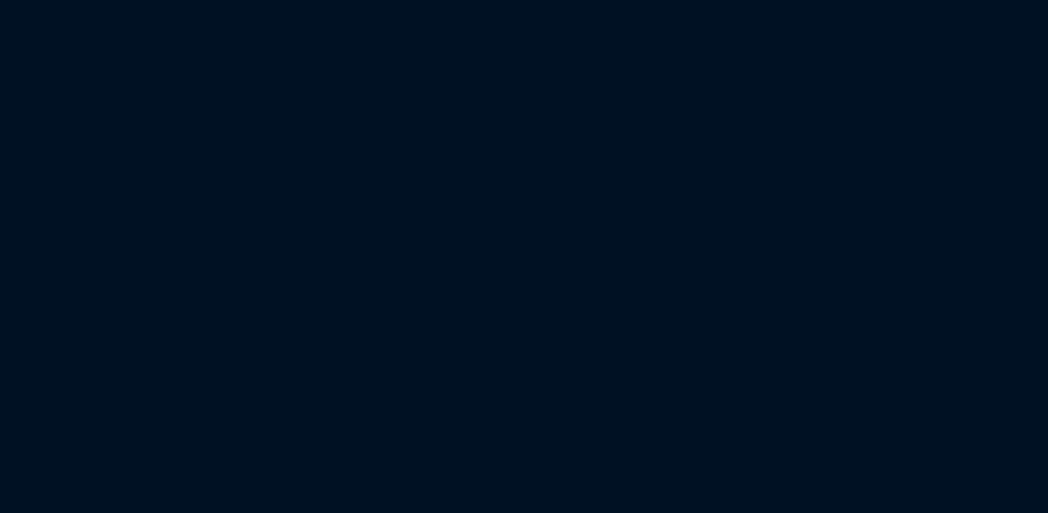
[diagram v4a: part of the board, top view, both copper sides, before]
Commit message: fix: VR1・VR2フットプリントをPCBに追加（スケマティックUUID紐付け）
スケマティックに対応するPCBフットプリントが存在しなかったVR1・VR2
(PSN_TRX:Potentiometer_TOCOS_GF063P_Vertical) をステージングエリア(250,290)
(270,290)に配置。Update PCB from Schematicで正しくリンクされる状態にした。

Co-Authored-By: Claude Sonnet 4.6 <noreply@anthropic.com>
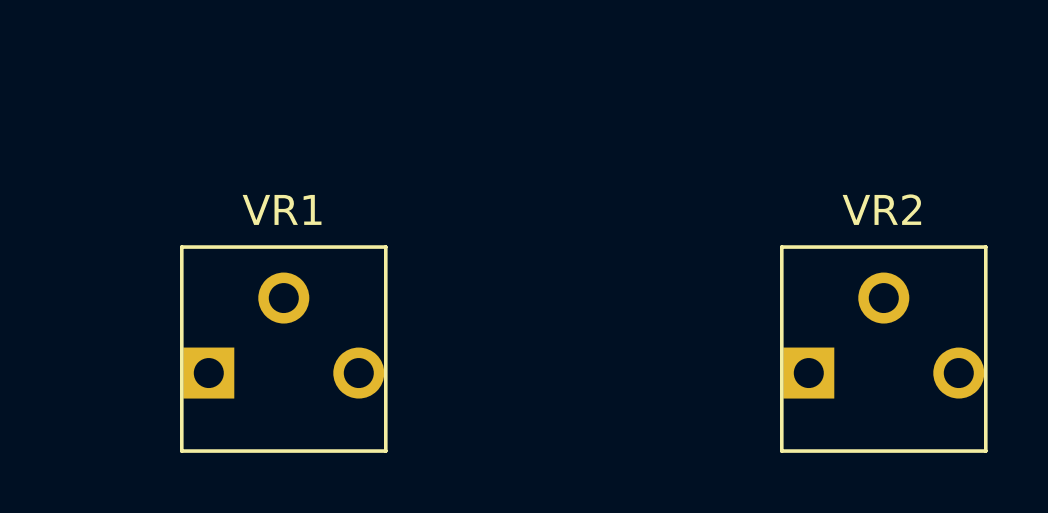
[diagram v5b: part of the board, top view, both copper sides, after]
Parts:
- added VR1: 10k, PSN_TRX:Potentiometer_TOCOS_GF063P_Vertical, F.Cu at (250.0, 290.0)
- added VR2: 10k, PSN_TRX:Potentiometer_TOCOS_GF063P_Vertical, F.Cu at (270.0, 290.0)
